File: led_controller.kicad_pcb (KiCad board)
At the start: 2 copper layers, 50 x 45 mm, 29 parts, among them IC1 ESP32-C3-MINI-1-N4X, J1 Screw_Terminal_01x02, J2 Screw_Terminal_01x02, J3 Conn_01x04_Pin, J4 Screw_Terminal_01x02, J6 Conn_01x03_Pin, Q1 AO3400A, U1 LM2596S-3.3

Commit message: Add files via upload
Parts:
- added C3: 100nF, Capacitor_SMD:C_1206_3216Metric_Pad1.33x1.80mm_HandSolder, F.Cu at (113.7, 45.2)
- moved C1 1.55 mm to (107.7, 45.2)
- moved C2 0.83 mm to (108.3, 42.0)
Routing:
- net GNDREF: track 99.5 -> 27.9 mm, vias 10 -> 1
- net EN: track 14.8 -> 30.0 mm, vias 0 -> 3
- net 3v3: track 140.3 -> 146.6 mm
- net TX: track 34.5 -> 36.6 mm
- net RX: track 29.6 -> 31.4 mm
- net IO5: track 17.7 -> 18.5 mm
- added copper zone on F.Cu, net GNDREF
- removed copper zone on F.Cu, net (none)

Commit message: Add files via upload
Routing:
- net GNDREF: track 27.9 -> 23.1 mm, vias 1 -> 8

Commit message: Add files via upload
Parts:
- moved R5 10.2 mm to (89.5, 38.2)
- moved R6 0.97 mm to (94.2, 50.3)
- moved R7 0.57 mm to (93.7, 53.9)
- moved J6 0.56 mm to (89.1, 44.8)
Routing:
- net Net-(J2-Pin_2): track 15.8 -> 4.98 mm
- net IO4: track 10.1 -> 20.3 mm
- net 3v3: track 146.6 -> 144.0 mm
- net Net-(J6-Pin_2): track 3.75 -> 5.15 mm
- net IO6: track 9.45 -> 8.57 mm
- net IO7: track 6.53 -> 7.09 mm
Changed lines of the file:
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@@
 	(footprint "Resistor_SMD:R_1206_3216Metric_Pad1.30x1.75mm_HandSolder"
 		(layer "B.Cu")
-		(at 97.69 44.18 90)
+		(at 89.46 38.16 90)
 		(descr "Resistor SMD 1206 (3216 Metric), square (rectangular) end terminal, IPC-7351 nominal with elongated pad for handsoldering. (Body size source: IPC-SM-782 page 72, https://www.pcb-3d.com/wordpress/wp-content/uploads/ipc-sm-782a_amendment_1_and_2.pdf), generated with kicad-footprint-generator")
 		(tags "resistor handsolder")
@@
 	(footprint "Resistor_SMD:R_1206_3216Metric_Pad1.30x1.75mm_HandSolder"
 		(layer "B.Cu")
-		(at 94.14 49.29)
+		(at 94.15 50.26)
 		(descr "Resistor SMD 1206 (3216 Metric), square (rectangular) end terminal, IPC-7351 nominal with elongated pad for handsoldering. (Body size source: IPC-SM-782 page 72, https://www.pcb-3d.com/wordpress/wp-content/uploads/ipc-sm-782a_amendment_1_and_2.pdf), generated with kicad-footprint-generator")
 		(tags "resistor handsolder")
@@
 	(footprint "Connector_JST:JST_EH_S3B-EH_1x03_P2.50mm_Horizontal"
 		(layer "B.Cu")
-		(at 89.62 44.9 -90)
+		(at 89.06 44.84 -90)
 		(descr "JST EH series connector, S3B-EH (http://www.jst-mfg.com/product/pdf/eng/eEH.pdf), generated with kicad-footprint-generator")
 		(tags "connector JST EH horizontal")
@@
 	(footprint "Resistor_SMD:R_1206_3216Metric_Pad1.30x1.75mm_HandSolder"
 		(layer "B.Cu")
-		(at 94.11 54.31)
+		(at 93.7 53.92)
 		(descr "Resistor SMD 1206 (3216 Metric), square (rectangular) end terminal, IPC-7351 nominal with elongated pad for handsoldering. (Body size source: IPC-SM-782 page 72, https://www.pcb-3d.com/wordpress/wp-content/uploads/ipc-sm-782a_amendment_1_and_2.pdf), generated with kicad-footprint-generator")
 		(tags "resistor handsolder")
@@
 	)
 	(gr_text "S1"
-		(at 80.1 50.86 270)
+		(at 80.55 50.89 270)
 		(layer "B.SilkS")
 		(effects
@@
 	)
 	(gr_text "S2"
-		(at 80.08 48.36 270)
+		(at 80.6 48.38 270)
 		(layer "B.SilkS")
 		(effects
@@
 	)
 	(gr_text "Com"
-		(at 81.8 45.397119 0)
+		(at 81.96 45.39 0)
 		(layer "B.SilkS")
 		(effects
@@
 	)
 	(via
-		(at 77.02 49.09)
+		(at 77.31 49.24)
 		(size 0.8)
 		(drill 0.6)
@@
 	)
 	(via
-		(at 77.02 51.14)
+		(at 77.31 51.29)
 		(size 0.8)
 		(drill 0.6)
@@
 	)
 	(via
-		(at 79.88 51.14)
+		(at 80.17 51.29)
 		(size 0.8)
 		(drill 0.6)
@@
 	)
 	(via
-		(at 79.88 47.12)
+		(at 80.17 47.27)
 		(size 0.8)
 		(drill 0.6)
@@
 	)
 	(via
-		(at 78.45 50.18)
+		(at 78.74 50.33)
 		(size 0.8)
 		(drill 0.6)
@@
 	)
 	(via
-		(at 77.02 47.12)
+		(at 77.31 47.27)
 		(size 0.8)
 		(drill 0.6)
@@
 	)
 	(via
-		(at 79.88 49.09)
+		(at 80.17 49.24)
 		(size 0.8)
 		(drill 0.6)
@@
 	)
 	(via
-		(at 78.45 48.13)
+		(at 78.74 48.28)
 		(size 0.8)
 		(drill 0.6)
@@
 		(start 96.55 63.14)
 		(end 90.57 63.14)
-		(width 0.257)
+		(width 0.5)
 		(layer "F.Cu")
 		(net 3)
@@
 	)
 	(segment
+		(start 112.62 41.42)
+		(end 110.94 39.74)
+		(width 0.5)
+		(layer "B.Cu")
+		(net 3)
+	)
+	(segment
 		(start 112.66 42.12)
-		(end 111.34 43.44)
+		(end 112.64 42.1)
 		(width 0.5)
 		(layer "B.Cu")
@@
 	)
 	(segment
+		(start 110.94 39.74)
+		(end 107.53 39.74)
+		(width 0.5)
+		(layer "B.Cu")
+		(net 3)
+	)
+	(segment
 		(start 75.84 36.86)
 		(end 78.94 36.86)
@@
 	)
 	(segment
-		(start 111.34 43.44)
-		(end 107.95 43.44)
-		(width 0.5)
-		(layer "B.Cu")
-		(net 3)
-	)
-	(segment
-		(start 107.53 43.02)
-		(end 107.53 39.74)
-		(width 0.5)
-		(layer "B.Cu")
-		(net 3)
-	)
-	(segment
 		(start 73.46 63.02)
 		(end 77.69 67.25)
@@
 	)
 	(segment
+		(start 112.64 42.1)
+		(end 112.64 41.42)
+		(width 0.5)
+		(layer "B.Cu")
+		(net 3)
+	)
+	(segment
 		(start 80.69 67.25)
 		(end 80.7 67.26)
@@
 		(start 70.88 51.93)
 		(end 70.88 41.82)
-		(width 0.5)
-		(layer "B.Cu")
-		(net 3)
-	)
-	(segment
-		(start 107.95 43.44)
-		(end 107.53 43.02)
 		(width 0.5)
 		(layer "B.Cu")
@@
 	)
 	(segment
-		(start 97.71 45.75)
-		(end 97.69 45.73)
-		(width 0.2)
+		(start 98.06 49.52)
+		(end 98.06 53.2)
+		(width 0.257)
 		(layer "B.Cu")
 		(net 8)
 	)
 	(segment
-		(start 98.06 53.2)
-		(end 97.71 52.85)
-		(width 0.2)
+		(start 89.46 39.71)
+		(end 89.46 42.14)
+		(width 0.257)
 		(layer "B.Cu")
 		(net 8)
 	)
 	(segment
-		(start 97.71 52.85)
-		(end 97.71 45.75)
+		(start 89.46 42.14)
+		(end 94.35 47.03)
+		(width 0.257)
+		(layer "B.Cu")
+		(net 8)
+	)
+	(segment
+		(start 94.35 47.03)
+		(end 95.59 47.03)
+		(width 0.257)
+		(layer "B.Cu")
+		(net 8)
+	)
+	(segment
+		(start 98.07 49.51)
+		(end 98.06 49.52)
+		(width 0.257)
+		(layer "B.Cu")
+		(net 8)
+	)
+	(segment
+		(start 95.59 47.03)
+		(end 98.07 49.51)
 		(width 0.257)
 		(layer "B.Cu")
@@
 	)
 	(segment
-		(start 93.74 38.52)
-		(end 89.46 34.24)
-		(width 0.257)
-		(layer "B.Cu")
-		(net 37)
-	)
-	(segment
-		(start 95.28 42.63)
-		(end 93.74 41.09)
-		(width 0.257)
-		(layer "B.Cu")
-		(net 37)
-	)
-	(segment
-		(start 89.46 34.24)
-		(end 89.46 31.63)
-		(width 0.257)
-		(layer "B.Cu")
-		(net 37)
-	)
-	(segment
-		(start 93.74 41.09)
-		(end 93.74 38.52)
-		(width 0.257)
-		(layer "B.Cu")
-		(net 37)
-	)
-	(segment
-		(start 97.69 42.63)
-		(end 95.28 42.63)
+		(start 89.46 31.63)
+		(end 89.46 36.61)
 		(width 0.257)
 		(layer "B.Cu")
@@
 	(segment
 		(start 95.66 56.19)
-		(end 95.66 54.31)
+		(end 95.66 54.33)
+		(width 0.257)
+		(layer "B.Cu")
+		(net 38)
+	)
+	(segment
+		(start 95.66 54.33)
+		(end 95.25 53.92)
 		(width 0.257)
 		(layer "B.Cu")
@@
 	(segment
 		(start 95.69 53.17)
-		(end 95.69 50.79)
+		(end 95.69 52.13)
 		(width 0.257)
 		(layer "F.Cu")
@@
 		(net 39)
 	)
-	(segment
-		(start 95.69 50.79)
-		(end 95.65 50.75)
-		(width 0.2)
-		(layer "F.Cu")
-		(net 39)
-	)
 	(via
-		(at 95.65 50.75)
+		(at 95.69 52.13)
 		(size 0.6)
 		(drill 0.3)
@@
 	)
 	(segment
-		(start 95.65 50.75)
-		(end 95.65 49.330001)
+		(start 95.69 50.270001)
+		(end 95.700001 50.26)
+		(width 0.257)
+		(layer "B.Cu")
+		(net 39)
+	)
+	(segment
+		(start 95.69 52.13)
+		(end 95.69 50.270001)
+		(width 0.257)
+		(layer "B.Cu")
+		(net 39)
+	)
+	(segment
+		(start 95.69 52.13)
+		(end 95.65 52.09)
 		(width 0.257)
 		(layer "B.Cu")
@@
 	)
 	(segment
-		(start 89.62 49.9)
-		(end 89.62 51.37)
+		(start 89.06 49.84)
+		(end 89.06 50.82)
 		(width 0.257)
 		(layer "B.Cu")
@@
 	)
 	(segment
-		(start 89.62 51.37)
-		(end 92.56 54.31)
+		(start 89.06 50.82)
+		(end 92.15 53.91)
 		(width 0.257)
 		(layer "B.Cu")
@@
 	)
 	(segment
-		(start 90.699999 47.4)
-		(end 92.589999 49.29)
+		(start 92.15 53.91)
+		(end 92.15 53.92)
+		(width 0.257)
+		(layer "B.Cu")
+		(net 40)
+	)
+	(segment
+		(start 92.599999 49.579999)
+		(end 90.36 47.34)
 		(width 0.257)
 		(layer "B.Cu")
@@
 	)
 	(segment
-		(start 89.62 47.4)
-		(end 90.699999 47.4)
-		(width 0.257)
-		(layer "B.Cu")
+		(start 90.36 47.34)
+		(end 89.06 47.34)
+		(width 0.257)
+		(layer "B.Cu")
+		(net 41)
+	)
+	(segment
+		(start 92.599999 50.26)
+		(end 92.599999 49.579999)
+		(width 0.257)
+		(layer "B.Cu")

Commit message: Add files via upload
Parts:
- moved S1 0.65 mm to (110.6, 37.9)
- moved J4 0.20 mm to (106.0, 31.8)
- moved J1 0.20 mm to (83.1, 31.8)
- moved J2 0.20 mm to (94.5, 31.8)
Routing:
- net VCC: track 43.1 -> 40.4 mm
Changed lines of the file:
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@@
 		(tags "resistor handsolder")
 		(property "Reference" "R2"
-			(at -1.63 -1.8 90)
+			(at -2.37 -1.65 90)
 			(layer "F.SilkS")
 			(effects
 				(font
-					(size 1 1)
+					(size 0.8 0.8)
 					(thickness 0.15)
 				)
@@
 		(tags "SOT TO_SOT_SMD")
 		(property "Reference" "Q1"
-			(at 1.58 1.31 180)
+			(at 1.52 1.84 180)
 			(layer "F.SilkS")
 			(effects
@@
 	(footprint "TerminalBlock:TerminalBlock_bornier-2_P5.08mm"
 		(layer "F.Cu")
-		(at 94.54 31.63 180)
+		(at 94.53 31.83 180)
 		(descr "simple 2-pin terminal block, pitch 5.08mm, revamped version of bornier2")
 		(tags "terminal block bornier2")
@@
 	(footprint "TerminalBlock:TerminalBlock_bornier-2_P5.08mm"
 		(layer "F.Cu")
-		(at 83.11 31.63 180)
+		(at 83.1 31.83 180)
 		(descr "simple 2-pin terminal block, pitch 5.08mm, revamped version of bornier2")
 		(tags "terminal block bornier2")
@@
 		(tags "capacitor handsolder")
 		(property "Reference" "C2"
-			(at 3.48 -0.06 0)
+			(at 3.27 -0.45 0)
 			(layer "F.SilkS")
 			(effects
 				(font
-					(size 1 1)
+					(size 0.8 0.8)
 					(thickness 0.15)
 				)
@@
 	(footprint "TerminalBlock:TerminalBlock_bornier-2_P5.08mm"
 		(layer "F.Cu")
-		(at 106 31.63 180)
+		(at 105.97 31.83 180)
 		(descr "simple 2-pin terminal block, pitch 5.08mm, revamped version of bornier2")
 		(tags "terminal block bornier2")
@@
 	(footprint "desk:KMR_2"
 		(layer "F.Cu")
-		(at 110.46 37.23)
+		(at 110.57 37.87)
 		(descr "KMR_2")
 		(tags "Switch")
@@
 		(tags "capacitor handsolder")
 		(property "Reference" "Cin1"
-			(at 0 -1.850001 0)
+			(at 1.32 -1.7 0)
 			(layer "F.SilkS")
 			(effects
@@
 	)
 	(gr_text "GND"
-		(at 87.45 70.85 0)
+		(at 87.53 71.18 0)
 		(layer "F.SilkS")
 		(effects
@@
 	)
 	(gr_text "TX"
-		(at 82.292857 70.95 0)
+		(at 82.3 71.26 0)
 		(layer "F.SilkS")
 		(effects
@@
 	)
 	(gr_text "3v3"
-		(at 78.91 70.92 0)
+		(at 78.91 71.28 0)
 		(layer "F.SilkS")
 		(effects
@@
 	)
 	(gr_text "RX"
-		(at 84.67381 70.9 0)
+		(at 84.69 71.25 0)
 		(layer "F.SilkS")
 		(effects
@@
 	)
 	(segment
+		(start 83.1 32.1)
+		(end 83.58 32.1)
+		(width 0.2)
+		(layer "F.Cu")
+		(net 1)
+	)
+	(segment
 		(start 93.38 42.9625)
 		(end 93.38 38.3075)
@@
 	)
 	(segment
-		(start 93.4575 38.23)
-		(end 93.4575 38.0775)
-		(width 0.2)
+		(start 94.54 32.09)
+		(end 94.53 32.1)
+		(width 1)
 		(layer "F.Cu")
 		(net 1)
 	)
 	(segment
-		(start 93.3875 42.97)
-		(end 93.38 42.9625)
-		(width 0.5)
+		(start 93.4575 38.23)
+		(end 93.4575 38.0775)
+		(width 0.2)
 		(layer "F.Cu")
 		(net 1)
@@
 	)
 	(segment
-		(start 83.11 31.63)
-		(end 83.11 29.16)
-		(width 1)
+		(start 93.3875 42.97)
+		(end 93.38 42.9625)
+		(width 0.5)
 		(layer "F.Cu")
 		(net 1)
 	)
 	(segment
-		(start 93.86 28.44)
-		(end 94.54 29.12)
-		(width 1)
+		(start 94.54 36.42)
+		(end 93.4575 37.5025)
+		(width 0.5)
 		(layer "F.Cu")
 		(net 1)
@@
 	)
 	(segment
-		(start 83.11 29.16)
-		(end 83.83 28.44)
-		(width 1)
+		(start 83.1 32.1)
+		(end 83.11 32.11)
+		(width 0.2)
 		(layer "F.Cu")
 		(net 1)
@@
 	)
 	(segment
-		(start 93.4575 38.0775)
-		(end 93.4575 37.5025)
+		(start 93.4575 37.5025)
+		(end 93.4575 38.0775)
 		(width 0.5)
 		(layer "F.Cu")
@@
 	)
 	(segment
-		(start 94.54 29.12)
-		(end 94.54 31.63)
+		(start 93.38 38.3075)
+		(end 93.3875 38.3)
+		(width 0.5)
+		(layer "F.Cu")
+		(net 1)
+	)
+	(segment
+		(start 93.86 28.44)
+		(end 94.54 29.12)
 		(width 1)
 		(layer "F.Cu")
@@
 	)
 	(segment
-		(start 93.38 38.3075)
-		(end 93.3875 38.3)
-		(width 0.5)
+		(start 83.11 29.16)
+		(end 83.83 28.44)
+		(width 1)
 		(layer "F.Cu")
 		(net 1)
 	)
 	(segment
-		(start 93.345146 32.824854)
-		(end 94.54 31.63)
-		(width 0.2)
+		(start 83.11 32.09)
+		(end 83.11 29.16)
+		(width 1)
 		(layer "F.Cu")
 		(net 1)
 	)
 	(segment
-		(start 94.54 36.42)
-		(end 94.54 31.63)
+		(start 94.54 32.11)
+		(end 94.54 36.42)
 		(width 0.5)
 		(layer "F.Cu")
@@
 	)
 	(segment
-		(start 83.11 31.63)
-		(end 84.02 32.54)
-		(width 0.2)
+		(start 94.54 29.12)
+		(end 94.54 32.09)
+		(width 1)
+		(layer "F.Cu")
+		(net 1)
+	)
+	(segment
+		(start 94.53 32.1)
+		(end 94.54 32.11)
+		(width 0.5)
 		(layer "F.Cu")
 		(net 1)
 	)
 	(segment
-		(start 83.11 31.63)
-		(end 83.11 32.83)
+		(start 94.07 32.1)
+		(end 94.53 32.1)
 		(width 0.2)
 		(layer "F.Cu")
@@
 	)
 	(segment
-		(start 93.4575 37.5025)
-		(end 94.54 36.42)
-		(width 0.5)
+		(start 83.1 32.1)
+		(end 83.11 32.09)
+		(width 1)
 		(layer "F.Cu")
 		(net 1)
@@
 	)
 	(segment
-		(start 100.92 32.98)
-		(end 103.97 36.03)
+		(start 100.92 31.63)
+		(end 100.92 32.09)
+		(width 0.7)
+		(layer "F.Cu")
+		(net 31)
+	)
+	(segment
+		(start 100.92 32.09)
+		(end 100.91 32.1)
 		(width 0.7)
 		(layer "F.Cu")
@@
 	)
 	(segment
-		(start 100.92 31.63)
-		(end 100.92 32.98)
+		(start 100.91 32.97)
+		(end 103.97 36.03)
+		(width 0.7)
+		(layer "F.Cu")
+		(net 31)
+	)
+	(segment
+		(start 100.91 32.1)
+		(end 100.91 32.97)
 		(width 0.7)
 		(layer "F.Cu")
@@
 	)
 	(segment
+		(start 108.52 37.07)
+		(end 107.54 37.07)
+		(width 0.257)
+		(layer "F.Cu")
+		(net 33)
+	)
+	(segment
 		(start 103.33 48.57)
 		(end 103.33 47.26)
@@
 	)
 	(segment
-		(start 107.52 36.43)
-		(end 108.41 36.43)
-		(width 0.2)
+		(start 107.54 37.07)
+		(end 107.52 37.09)
+		(width 0.257)
 		(layer "F.Cu")
 		(net 33)
@@
 	)
 	(via
-		(at 107.52 36.43)
+		(at 107.52 37.09)
 		(size 0.6)
 		(drill 0.3)
@@
 	)
 	(segment
-		(start 103.33 45.75)
-		(end 104.87 44.21)
+		(start 115.23 43.58)
+		(end 115.23 38.59)
 		(width 0.257)
 		(layer "B.Cu")
@@
 	)
 	(segment
-		(start 104.87 44.21)
-		(end 104.87 40.4)
+		(start 107.52 37.09)
+		(end 107.52 37.75)
 		(width 0.257)
 		(layer "B.Cu")
@@
 	)
 	(segment
-		(start 115.23 43.58)
-		(end 115.23 38.59)
+		(start 115.23 38.59)
+		(end 113.07 36.43)
 		(width 0.257)
 		(layer "B.Cu")
@@
 	)
 	(segment
-		(start 113.07 36.43)
-		(end 108.08 36.43)
+		(start 104.87 40.4)
+		(end 104.87 44.21)
 		(width 0.257)
 		(layer "B.Cu")
@@
 	(segment
 		(start 107.52 37.75)
-		(end 107.52 36.43)
+		(end 104.87 40.4)
 		(width 0.257)
 		(layer "B.Cu")
@@
 	)
 	(segment
-		(start 115.23 38.59)
-		(end 113.07 36.43)
+		(start 108.18 36.43)
+		(end 107.52 37.09)
 		(width 0.257)
 		(layer "B.Cu")
@@
 	)
 	(segment
-		(start 104.87 40.4)
-		(end 107.52 37.75)
+		(start 113.07 36.43)
+		(end 108.18 36.43)
 		(width 0.257)
 		(layer "B.Cu")
@@
 	)
 	(segment
-		(start 103.33 47.26)
+		(start 104.87 44.21)
 		(end 103.33 45.75)
 		(width 0.257)
@@
 	)
 	(segment
-		(start 108.08 36.43)
-		(end 107.52 36.43)
-		(width 0.2)
+		(start 103.33 45.75)
+		(end 103.33 47.26)
+		(width 0.257)
 		(layer "B.Cu")
 		(net 33)
@@
 	)
 	(segment
-		(start 112.51 36.43)
-		(end 114.65 36.43)
+		(start 114.76 36.54)
+		(end 113.15 36.54)
+		(width 0.2)
+		(layer "F.Cu")
+		(net 35)
+	)
+	(segment
+		(start 113.15 36.54)
+		(end 112.62 37.07)
 		(width 0.2)
 		(layer "F.Cu")

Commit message: Add files via upload
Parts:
- Cin1, Cout2: footprint Capacitor_SMD:C_1206_3216Metric_Pad1.33x1.80mm_HandSolder -> Capacitor_SMD:CP_Elec_6.3x5.8
- moved Cin1 2.76 mm to (92.6, 39.6)
- moved Cin2 2.70 mm to (94.5, 45.6)
- moved Cout2 1.15 mm to (77.3, 60.2)
- moved Cout1 1.11 mm to (83.4, 61.4)
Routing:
- net GNDREF: track 23.1 -> 19.1 mm
- net VCC: track 40.4 -> 41.9 mm

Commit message: Add files via upload
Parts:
- Cin1: footprint Capacitor_SMD:CP_Elec_6.3x5.8 -> Capacitor_SMD:CP_Elec_8x10
- moved Cin2 2.37 mm to (94.1, 48.0), turned to -90 degrees
- moved J6 1.77 mm to (89.5, 46.5)
- moved Cin1 0.90 mm to (92.7, 40.5)
- moved U1 0.70 mm to (80.0, 47.4)
- moved R7 0.68 mm to (94.4, 54.1)
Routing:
- net GNDREF: track 19.1 -> 20.4 mm
- net VCC: track 41.9 -> 43.1 mm
- net Net-(J6-Pin_3): track 5.36 -> 4.32 mm
- net Net-(J6-Pin_2): track 5.15 -> 4.25 mm
- net 3v3: track 144.0 -> 143.1 mm
- net Net-(D1-K): track 41.8 -> 42.5 mm
- net IO7: track 7.09 -> 6.51 mm

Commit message: Add files via upload
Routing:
- net GNDREF: vias 8 -> 12
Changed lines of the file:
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@@
 	(via
 		(at 77.31 49.24)
-		(size 0.8)
-		(drill 0.6)
+		(size 1)
+		(drill 0.8)
 		(layers "F.Cu" "B.Cu")
 		(net 2)
@@
 	(via
 		(at 77.31 51.29)
-		(size 0.8)
-		(drill 0.6)
+		(size 1)
+		(drill 0.8)
+		(layers "F.Cu" "B.Cu")
+		(net 2)
+	)
+	(via
+		(at 80.17 45.52)
+		(size 1)
+		(drill 0.8)
+		(layers "F.Cu" "B.Cu")
+		(net 2)
+	)
+	(via
+		(at 78.74 52.59)
+		(size 1)
+		(drill 0.8)
 		(layers "F.Cu" "B.Cu")
 		(net 2)
@@
 	(via
 		(at 80.17 51.29)
-		(size 0.8)
-		(drill 0.6)
+		(size 1)
+		(drill 0.8)
 		(layers "F.Cu" "B.Cu")
 		(net 2)
@@
 	(via
 		(at 80.17 47.27)
-		(size 0.8)
-		(drill 0.6)
+		(size 1)
+		(drill 0.8)
 		(layers "F.Cu" "B.Cu")
 		(net 2)
@@
 	(via
 		(at 78.74 50.33)
-		(size 0.8)
-		(drill 0.6)
+		(size 1)
+		(drill 0.8)
+		(layers "F.Cu" "B.Cu")
+		(net 2)
+	)
+	(via
+		(at 78.74 46.29)
+		(size 1)
+		(drill 0.8)
 		(layers "F.Cu" "B.Cu")
 		(net 2)
@@
 	(via
 		(at 77.31 47.27)
-		(size 0.8)
-		(drill 0.6)
+		(size 1)
+		(drill 0.8)
 		(layers "F.Cu" "B.Cu")
 		(net 2)
@@
 	(via
 		(at 80.17 49.24)
-		(size 0.8)
-		(drill 0.6)
+		(size 1)
+		(drill 0.8)
+		(layers "F.Cu" "B.Cu")
+		(net 2)
+	)
+	(via
+		(at 77.31 45.49)
+		(size 1)
+		(drill 0.8)
 		(layers "F.Cu" "B.Cu")
 		(net 2)
@@
 	(via
 		(at 78.74 48.28)
-		(size 0.8)
-		(drill 0.6)
+		(size 1)
+		(drill 0.8)
 		(layers "F.Cu" "B.Cu")
 		(net 2)

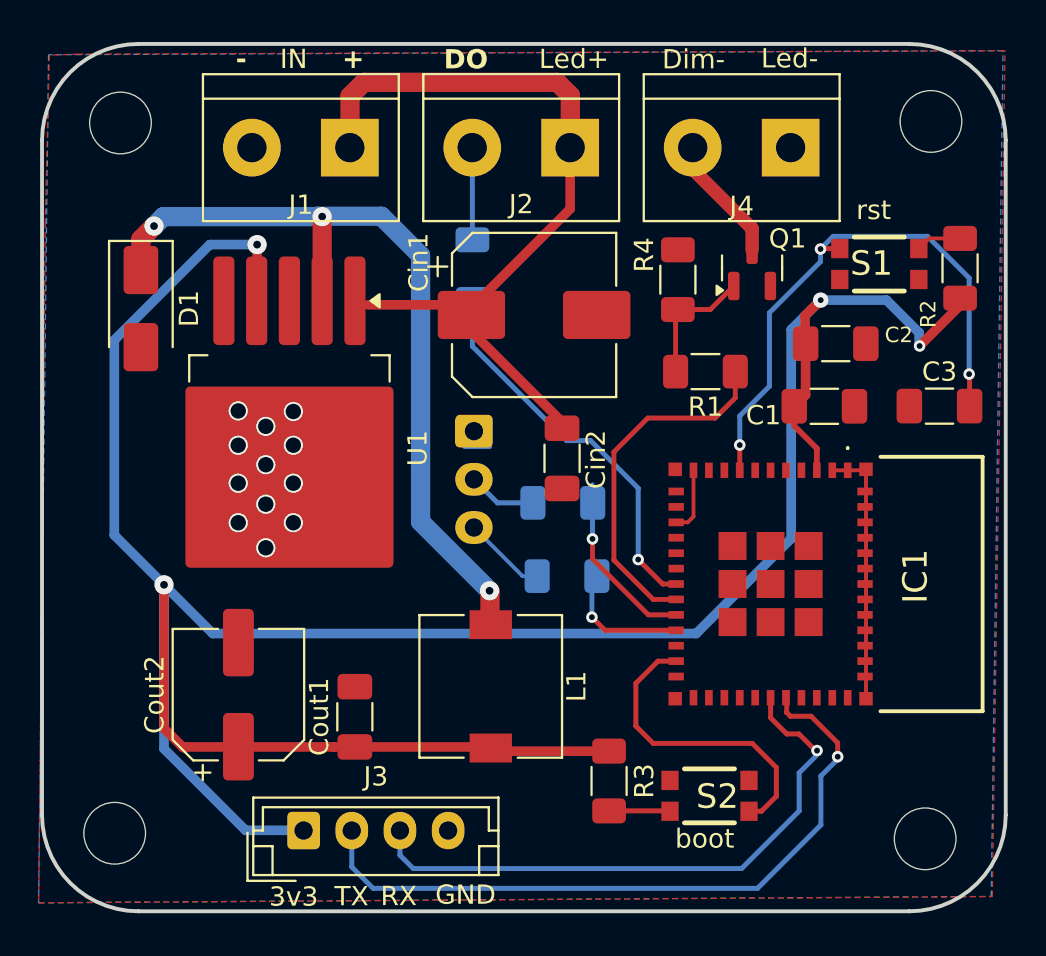
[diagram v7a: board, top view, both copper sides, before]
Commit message: kicad10 and modified antenna
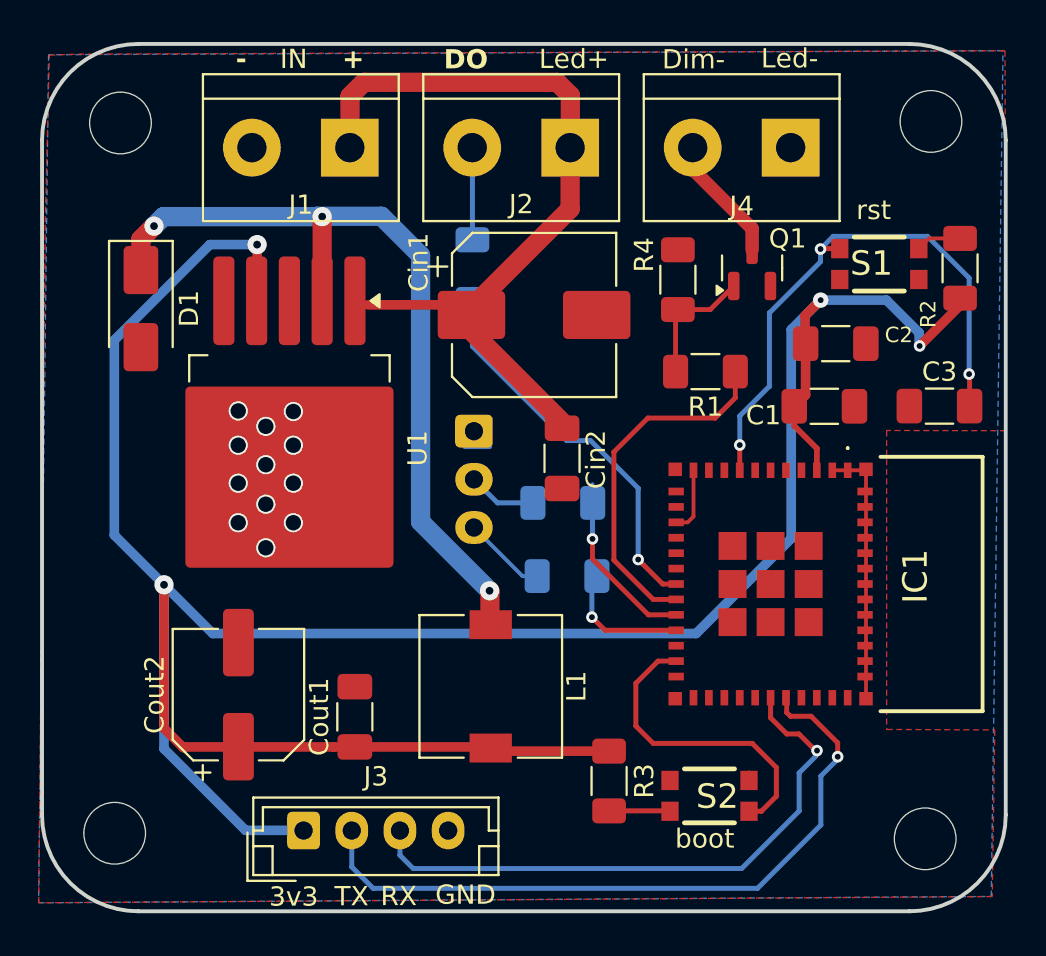
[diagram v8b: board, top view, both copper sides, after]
